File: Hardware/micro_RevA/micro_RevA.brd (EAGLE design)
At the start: 50 x 50 mm, 22 parts, among them IC1 TLC59711, Q1 CSTCR6M00G53Z

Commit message: Readme changes, update to micro board
Added trace sizing to readme, began running traces for micro board (it's
busy).
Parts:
- moved R3 0.90 mm to (18.3, 33.0)
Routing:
- net A_2: track 0.00 -> 29.9 mm, vias 0 -> 1
- net A_3: track 0.00 -> 28.8 mm, vias 0 -> 1
- net A_1: track 0.00 -> 28.7 mm, vias 0 -> 1
- net VCC: track 26.2 -> 51.6 mm, vias 0 -> 1
- net P_1: track 0.00 -> 24.6 mm, vias 0 -> 1
- net P_3: track 0.00 -> 21.6 mm, vias 0 -> 1
- net P_2: track 0.00 -> 20.0 mm, vias 0 -> 1
- net T_3: track 0.00 -> 19.7 mm, vias 0 -> 1
- net T_2: track 0.00 -> 19.1 mm, vias 0 -> 1
- net T_1: track 0.00 -> 17.8 mm, vias 0 -> 1
- net GND: track 22.1 -> 26.1 mm
- net N$4: track 0.00 -> 2.10 mm

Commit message: WOW!! Almost forgot to connect data and clk lines
Good to catch the stupid shit early on.
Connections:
- net CLK: now also U$1.12
- net DATA: now also U$1.30
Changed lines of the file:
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@@
 <signal name="CLK">
 <contactref element="IC1" pad="10"/>
+<contactref element="U$1" pad="12"/>
+<wire x1="11.9258125" y1="28.3114125" x2="30.184" y2="19.5204" width="0" layer="19" extent="1-16"/>
 </signal>
 <signal name="DATA">
 <contactref element="IC1" pad="9"/>
+<contactref element="U$1" pad="30"/>
+<wire x1="12.38543125" y1="28.77103125" x2="22.784" y2="29.3204" width="0" layer="19" extent="1-16"/>
 </signal>
 <signal name="TX">

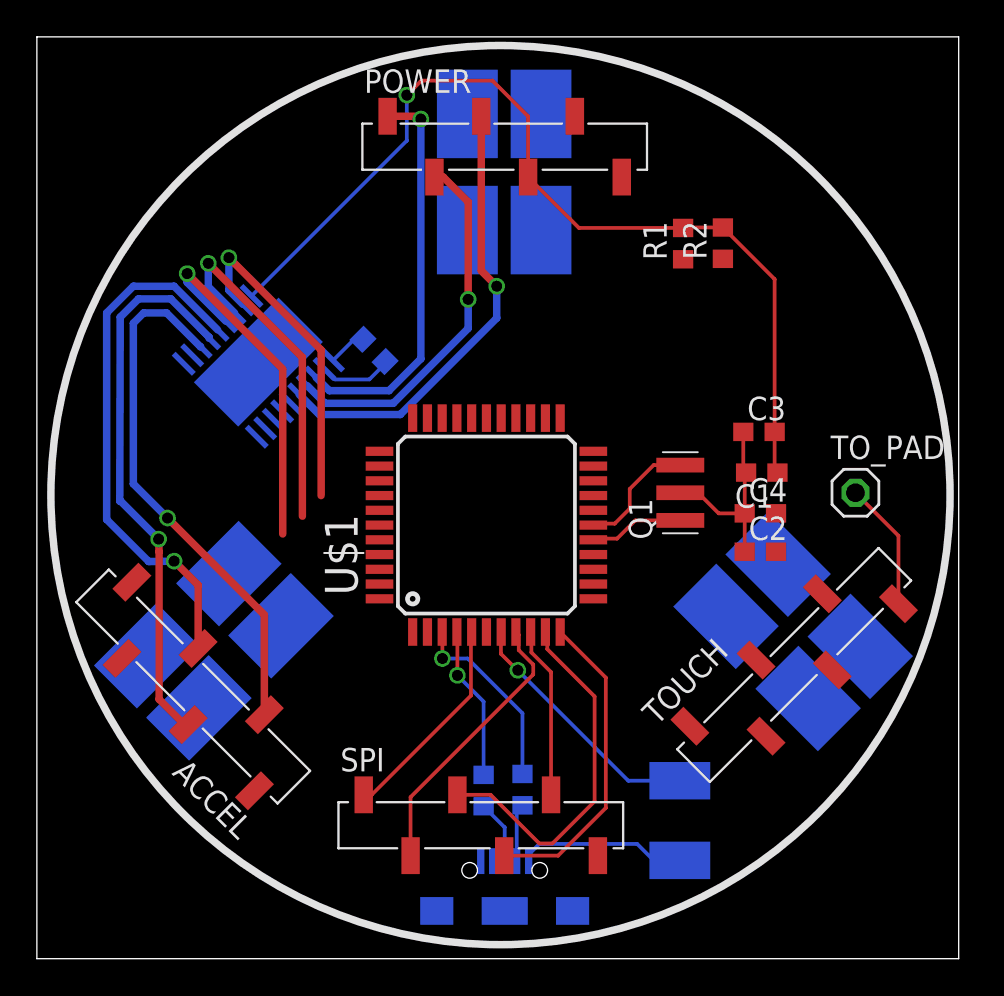
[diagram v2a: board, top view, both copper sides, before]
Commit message: Completed routing of microcontroller board
Everything is routed and passes drc. Still needs visual inspection.
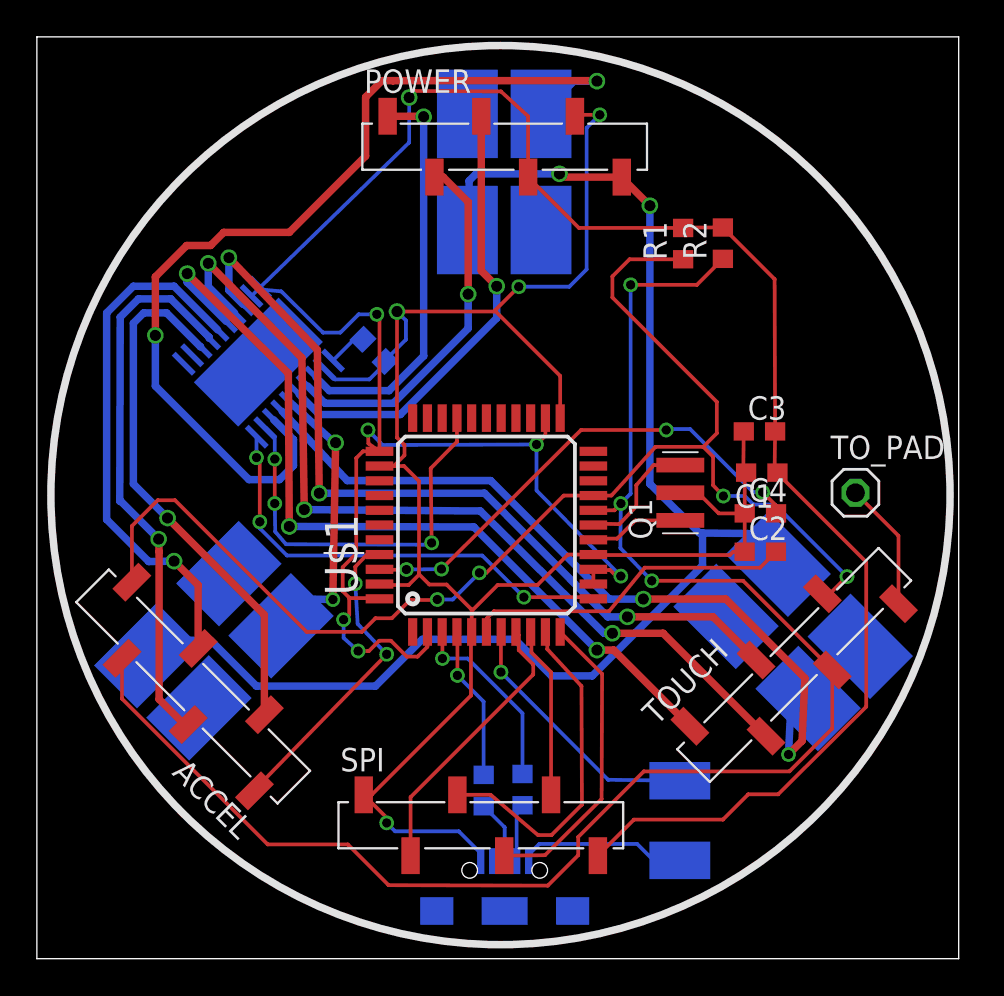
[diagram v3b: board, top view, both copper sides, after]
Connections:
- net VCC: now also U$1.13, U$1.14, U$1.2, U$1.24, U$1.44
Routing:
- net VCC: track 51.6 -> 142.8 mm, vias 1 -> 7
- net SCL: track 0.00 -> 88.2 mm, vias 0 -> 3
- net GND: track 26.1 -> 106.1 mm, vias 0 -> 4
- net VDD: track 0.00 -> 74.9 mm, vias 0 -> 2
- net SDA: track 0.00 -> 71.3 mm, vias 0 -> 4
- net N$7: track 0.00 -> 52.8 mm, vias 0 -> 2
- net N$6: track 0.00 -> 42.3 mm, vias 0 -> 2
- net T_2: track 19.1 -> 48.8 mm, vias 1 -> 3
- net T_1: track 17.8 -> 45.0 mm, vias 1 -> 3
- net N$3: track 0.00 -> 26.8 mm, vias 0 -> 4
- net T_3: track 19.7 -> 45.7 mm, vias 1 -> 3
- net CLK: track 0.00 -> 24.7 mm, vias 0 -> 3
- net DATA: track 0.00 -> 22.1 mm, vias 0 -> 3
- net N$8: track 0.00 -> 18.1 mm
- net N$9: track 0.00 -> 17.4 mm, vias 0 -> 2
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
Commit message: Finished micro and adjusted text of accel
MUST CHECK THAT TPLACE IS ON SILSCREEN OR SHIT!!!
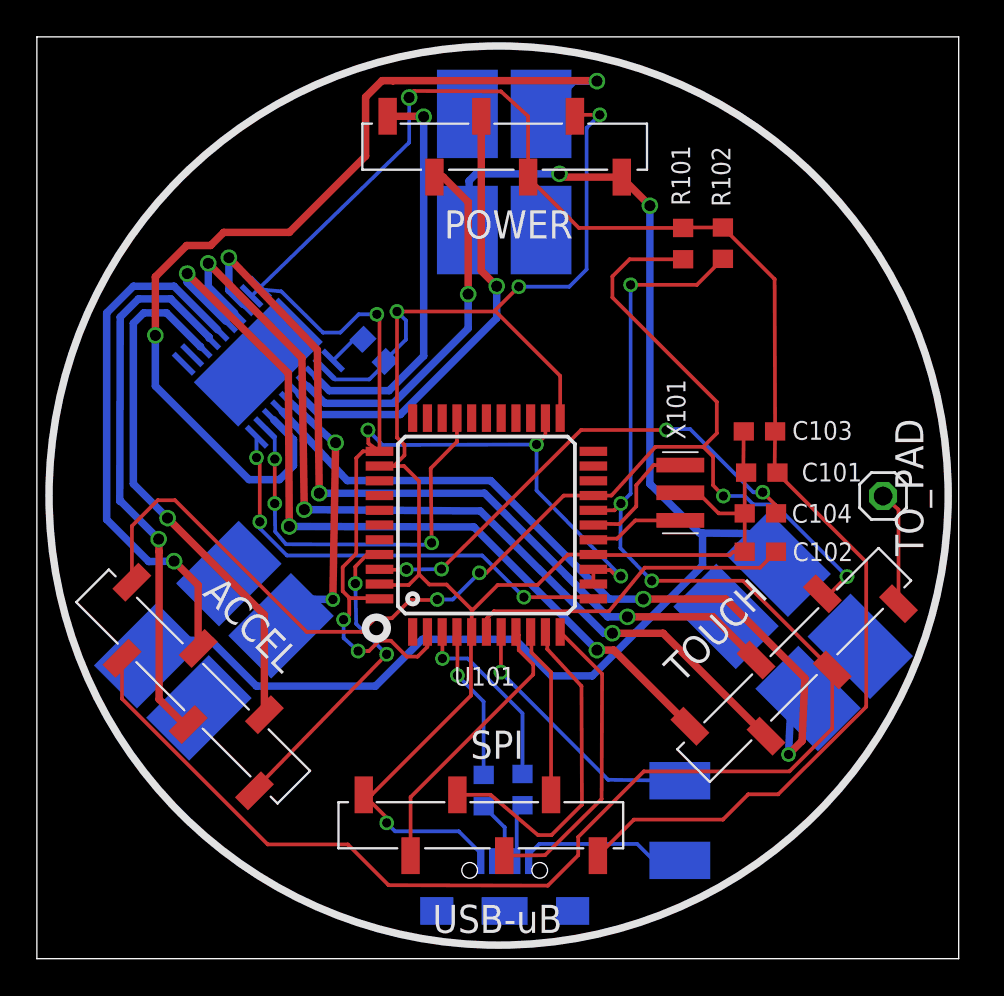
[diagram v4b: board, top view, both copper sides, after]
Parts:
- moved TO_PAD 1.51 mm to (45.9, 25.1)
- renumbered C1 to C101, C2 to C102, C3 to C103, C4 to C104, JP1 to USB-UB, R1 to R101, R2 to R102, R3 to R103, R4 to R104, R5 to R105
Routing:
- net TOUCH: track 6.99 -> 6.22 mm
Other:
- board text added: "F101"
- board text added: "U101"
- board text added: "U102"
- board text added: "USB-uB"
- board text added: "X101"
